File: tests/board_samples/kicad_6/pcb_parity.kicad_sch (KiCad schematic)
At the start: 4 parts

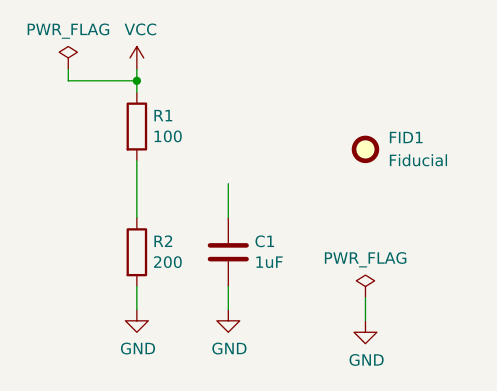
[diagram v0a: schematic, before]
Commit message: [PCB/SCH parity] Check for value and fields/properties
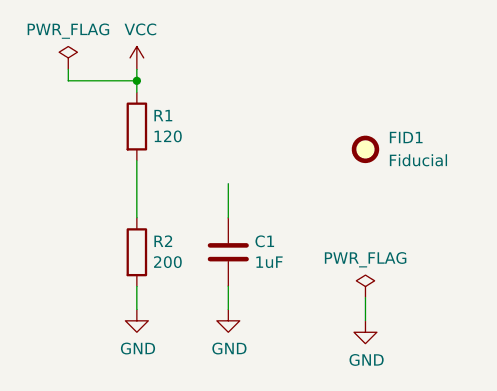
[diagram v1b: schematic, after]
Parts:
- R1: value 100 -> 120; footprint Resistor_SMD:R_0805_2012Metric -> Resistor_SMD:R_0603_2012Metric
- R2: Tolerance (none) -> 1%
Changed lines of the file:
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@@
       (effects (font (size 1.27 1.27)) (justify left))
     )
-    (property "Value" "100" (id 1) (at 90.678 57.023 0)
+    (property "Value" "120" (id 1) (at 90.678 57.023 0)
       (effects (font (size 1.27 1.27)) (justify left))
     )
-    (property "Footprint" "Resistor_SMD:R_0805_2012Metric" (id 2) (at 87.122 55.88 90)
+    (property "Footprint" "Resistor_SMD:R_0603_2012Metric" (id 2) (at 87.122 55.88 90)
       (effects (font (size 1.27 1.27)) hide)
     )
@@
       (effects (font (size 1.27 1.27)) hide)
     )
+    (property "Tolerance" "1%" (id 4) (at 88.9 69.85 0)
+      (effects (font (size 1.27 1.27)) hide)
+    )
     (pin "1")
     (pin "2")
@@
       (effects (font (size 1.27 1.27)) hide)
     )
-    (property "Datasheet" "~" (id 3) (at 99.06 69.85 0)
+    (property "Datasheet" "bogus.pdf" (id 3) (at 99.06 69.85 0)
       (effects (font (size 1.27 1.27)) hide)
     )
@@
     )
     (path "/00000000-0000-0000-0000-00005ebe8a2e"
-      (reference "R1") (unit 1) (value "100") (footprint "Resistor_SMD:R_0805_2012Metric")
+      (reference "R1") (unit 1) (value "120") (footprint "Resistor_SMD:R_0603_2012Metric")
     )
     (path "/00000000-0000-0000-0000-00005ebe8e9e"
